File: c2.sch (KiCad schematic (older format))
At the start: 0 parts

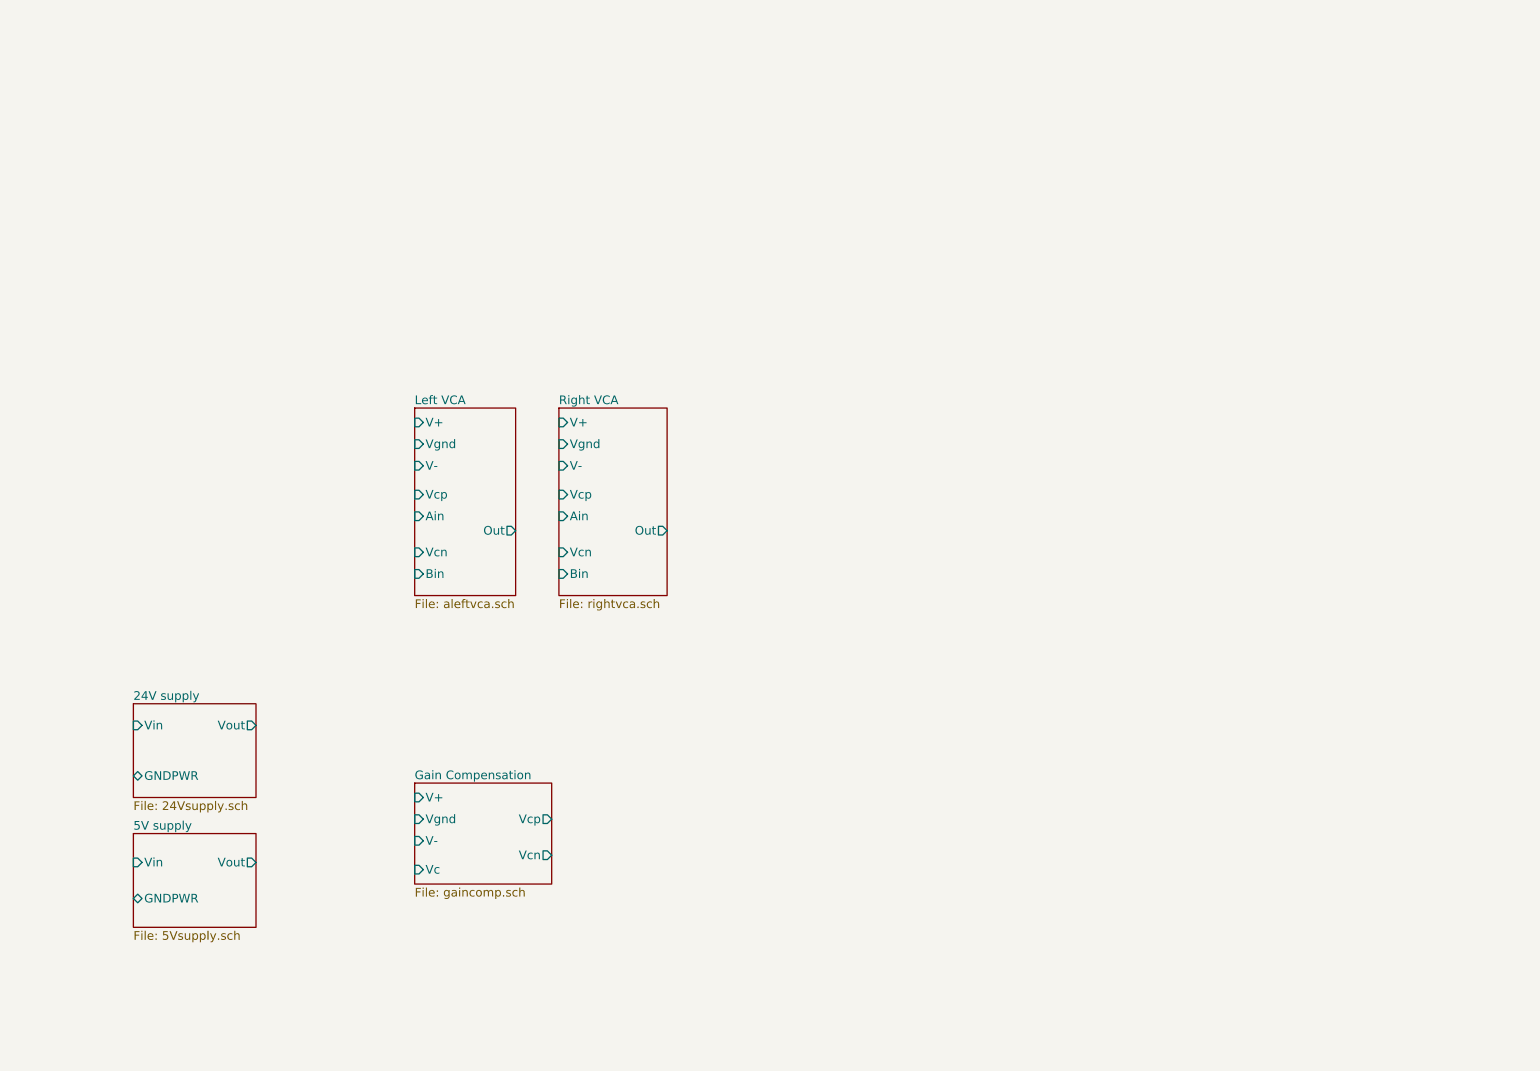
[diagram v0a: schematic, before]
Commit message: Added top-level connections
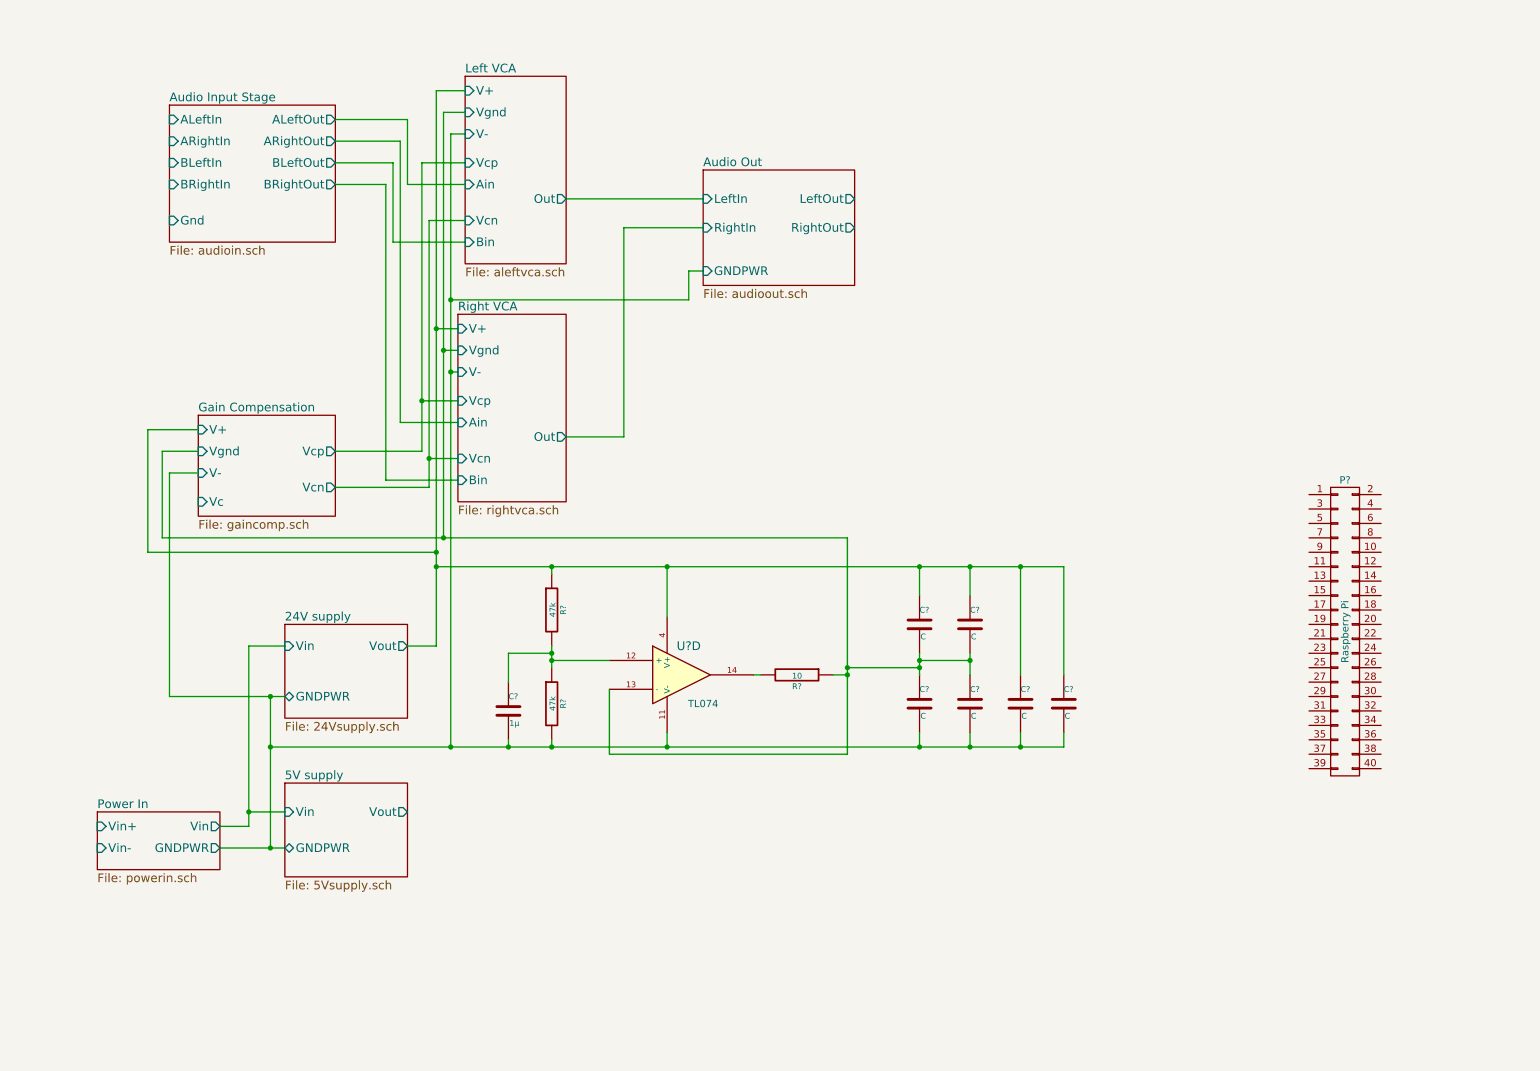
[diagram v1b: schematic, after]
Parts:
- added C?: 1µ, symbol C
- added C? (x6): C, symbol C
- added P?: Raspberry Pi, symbol CONN_02X20
- added R? (x2): 47k, symbol R
- added R?: 10, symbol R
- added U?: TL074, symbol TL074
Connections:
- net 24V supply/GNDPWR: now also C?.2, C?.2, C?.2, C?.2, C?.2, R?.2, U?.11 (V-)
- net 24V supply/Vout: now also C?.1, C?.1, C?.1, C?.1, R?.1, U?.4 (V+)
- net Gain Compensation/Vgnd: now also C?.1, C?.1, C?.2, C?.2, R?.1, U?.13 (-)
- new net: C?.1, R?.1, R?.2, U?.12 (+)
- new net: R?.2, U?.14

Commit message: Unknown changes
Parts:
- added CON? (x4): USB-MICRO-B, symbol USB-MICRO-B
- added R? (x6): R, symbol R
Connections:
- net 24V supply/GNDPWR: now also P?.14 (P14), P?.20 (P20), P?.25 (P25), P?.30 (P30), P?.34 (P34), P?.39 (P39), P?.6 (P6), P?.9 (P9), CON?.5 (GND), CON?.5 (GND), CON?.5 (GND), CON?.5 (GND), R?.2, R?.2, R?.2, R?.2, R?.2, R?.2
- net 5V supply/Vout: now also CON?.1 (VBUS)
- net Audio Input Stage/ALeftIn: now also CON?.2 (D-)
- net Audio Input Stage/ARightIn: now also CON?.3 (D+)
- net Audio Input Stage/BLeftIn: now also CON?.2 (D-)
- net Audio Input Stage/BRightIn: now also CON?.3 (D+)
- net Audio Out/LeftOut: now also CON?.2 (D-)
- net Audio Out/RightOut: now also CON?.3 (D+)
- net rp3v3: now reaches P?.1 (P1)
- net rp3v3: now also P?.17 (P17)
- net rp5v: now reaches P?.2 (P2)
- net rp5v: now also P?.4 (P4)
- net rpgpio2: now reaches P?.3 (P3)
- net rpgpio3: now reaches P?.5 (P5)
- new net: CON?.1 (VBUS), R?.1
- new net: CON?.6 (SHELL1), CON?.7 (SHELL2), CON?.8 (SHELL3), CON?.9 (SHELL4), R?.1 (x4)
- new net: CON?.1 (VBUS), CON?.1 (VBUS), R?.1
- no-connect marks 0 -> 36
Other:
- moved on the sheet: C?, P?, R?, U?D

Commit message: Some work
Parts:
- removed CON? (x4): USB-MICRO-B, symbol USB-MICRO-B
- removed R? (x6): R, symbol R
- removed U?: TL074, symbol TL074
- added C?: 1µ, symbol C
- added K?: mixpot, symbol CONN_3
- added P?: Raspberry Pi, symbol CONN_02X20
- added P?: rpipower, symbol CONN_2
- added P?: CONN_2, symbol CONN_2
- added P?: audioin, symbol CONN_4X2
- added P?: audioout, symbol CONN_2X2
- added R? (x2): 47k, symbol R
- added U?: TL074, symbol TL074
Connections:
- net 24V supply/GNDPWR: now also C?.2, P?.1, P?.1, P?.1 (P1), P?.14 (P14), P?.20 (P20), P?.25 (P25), P?.3, P?.3, P?.30 (P30), P?.34 (P34), P?.39 (P39), P?.5, P?.6 (P6), P?.7, P?.9 (P9), R?.2, U?.11 (V-)
- net 24V supply/Vout: now also R?.1, U?.4 (V+)
- net 5V supply/Vout: now also P?.2 (PM)
- net Audio Input Stage/ALeftIn: now also P?.2
- net Audio Input Stage/ARightIn: now also P?.4
- net Audio Input Stage/BLeftIn: now also P?.6
- net Audio Input Stage/BRightIn: now also P?.8
- net Audio Out/LeftOut: now also P?.2
- net Audio Out/RightOut: now also P?.4
- net Gain Compensation/Vc: now also K?.2 (PM)
- net Power In/Vin+: now also P?.2 (PM)
- net Power In/Vin-: now also P?.1 (P1)
- net rp3v3: now also P?.1 (P1), P?.17 (P17)
- net rp5v: now also P?.2 (P2), P?.4 (P4)
- net rpgpio2: now also P?.3 (P3)
- net rpgpio3: now also P?.5 (P5)
- net at P?.10 (P10): now also P?.10 (P10)
- net at P?.11 (P11): now also P?.11 (P11)
- net at P?.12 (P12): now also P?.12 (P12)
- net at P?.13 (P13): now also P?.13 (P13)
- net at P?.15 (P15): now also P?.15 (P15)
- net at P?.16 (P16): now also P?.16 (P16)
- net at P?.18 (P18): now also P?.18 (P18)
- net at P?.19 (P19): now also P?.19 (P19)
- net at P?.21 (P21): now also P?.21 (P21)
- net at P?.22 (P22): now also P?.22 (P22)
- net at P?.23 (P23): now also P?.23 (P23)
- net at P?.24 (P24): now also P?.24 (P24)
- net at P?.26 (P26): now also P?.26 (P26)
- net at P?.27 (P27): now also P?.27 (P27)
- net at P?.28 (P28): now also P?.28 (P28)
- net at P?.29 (P29): now also P?.29 (P29)
- net at P?.31 (P31): now also P?.31 (P31)
- net at P?.32 (P32): now also P?.32 (P32)
- net at P?.33 (P33): now also P?.33 (P33)
- net at P?.35 (P35): now also P?.35 (P35)
- net at P?.36 (P36): now also P?.36 (P36)
- net at P?.37 (P37): now also P?.37 (P37)
- net at P?.38 (P38): now also P?.38 (P38)
- net at P?.40 (P40): now also P?.40 (P40)
- net at P?.7 (P7): now also P?.7 (P7)
- net at P?.8 (P8): now also P?.8 (P8)
- net at C?.1, R?.1, R?.2: now also U?.3 (+)
- net at R?.2: now also U?.1
- net Gain Compensation/Vgnd renamed Audio Input Stage/Gnd
- net Audio Input Stage/Gnd: now also U?.2 (-)
- new net: K?.1 (P1), R?.2
- new net: C?.1, K?.3 (P3), R?.1
- no-connect marks 36 -> 60

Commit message: Ready for tapeout
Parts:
- removed P? (x2): Raspberry Pi, symbol CONN_02X20
- added C3, C4: 10u, symbol C
- added P1: CONN_5, symbol CONN_5
- added P5: amped, symbol CONN_4X2
- C10, C5, C6, C7, C8, C9: renamed from C?; value C -> 100n
- gave numbers to parts that had none: 13
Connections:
- net 24V supply/GNDPWR: now also P4.2, P4.4, P7.2, C4.2, P1.1; no longer P4.5, P4.7, P7.3
- net 24V supply/Vout: now also C3.1
- net Audio Input Stage/ALeftIn: now also P4.8; no longer P4.2
- net Audio Input Stage/ALeftOut: now also P5.8
- net Audio Input Stage/ARightIn: now also P4.7; no longer P4.4
- net Audio Input Stage/ARightOut: now also P5.7
- net Audio Input Stage/BLeftOut: now also P5.6
- net Audio Input Stage/BRightIn: now also P4.5; no longer P4.8
- net Audio Input Stage/BRightOut: now also P5.5
- net Audio Input Stage/Gnd: now also C3.2, C4.1, P5.1, P5.2, P5.3, P5.4
- net Audio Out/LeftOut: now also P7.4; no longer P7.2
- net Audio Out/RightOut: now also P7.3; no longer P7.4
- new net ADC/clk: P1.4
- new net ADC/miso: P1.3
- new net ADC/mosi: P1.2
- new net ADC/v3.3: P1.5
- no-connect marks 60 -> 0
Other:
- moved on the sheet: C1, C10, C2, C5, C6, C7, C8, C9, K1, P3, P4, P6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
